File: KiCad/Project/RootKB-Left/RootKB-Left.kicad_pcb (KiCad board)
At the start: 2 copper layers, 137.4 x 107.4 mm, 69 parts, among them J1 OLED-128x32, U1 Arduino_Pro_Micro, U2 TRRS

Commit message: add jblpcb order number location
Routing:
- added copper zone on B.Cu, net GND
- added copper zone on F.Cu, net GND
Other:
- board text added: "JLCJLCJLCJLC"
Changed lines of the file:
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@@
 		(layer "User.9")
 	)
+	(gr_text "JLCJLCJLCJLC"
+		(at 138.934292 116.834545 331)
+		(layer "B.SilkS")
+		(effects
+			(font
+				(size 1 1)
+				(thickness 0.25)
+				(bold yes)
+			)
+			(justify left bottom mirror)
+		)
+	)
 	(gr_text "by Matei Ionescu"
 		(at 127.988 113.0215 331)
@@
 		(net 64)
 	)
-	(group ""
-		(members "570610eb-6886-4a19-860b-f766abbdb514")
+	(zone
+		(net 32)
+		(net_name "GND")
+		(layers "F&B.Cu")
+		(hatch edge 0.5)
+		(connect_pads
+			(clearance 0)
+		)
+		(min_thickness 0.25)
+		(filled_areas_thickness no)
+		(fill yes
+			(thermal_gap 0.5)
+			(thermal_bridge_width 0.5)
+		)
+		(polygon
+			(pts
+				(xy 69.934292 32.634545) (xy 69.934292 152.634545) (xy 224.934292 152.634545) (xy 224.934292 32.634545)
+			)
+		)
 	)
 	(group ""

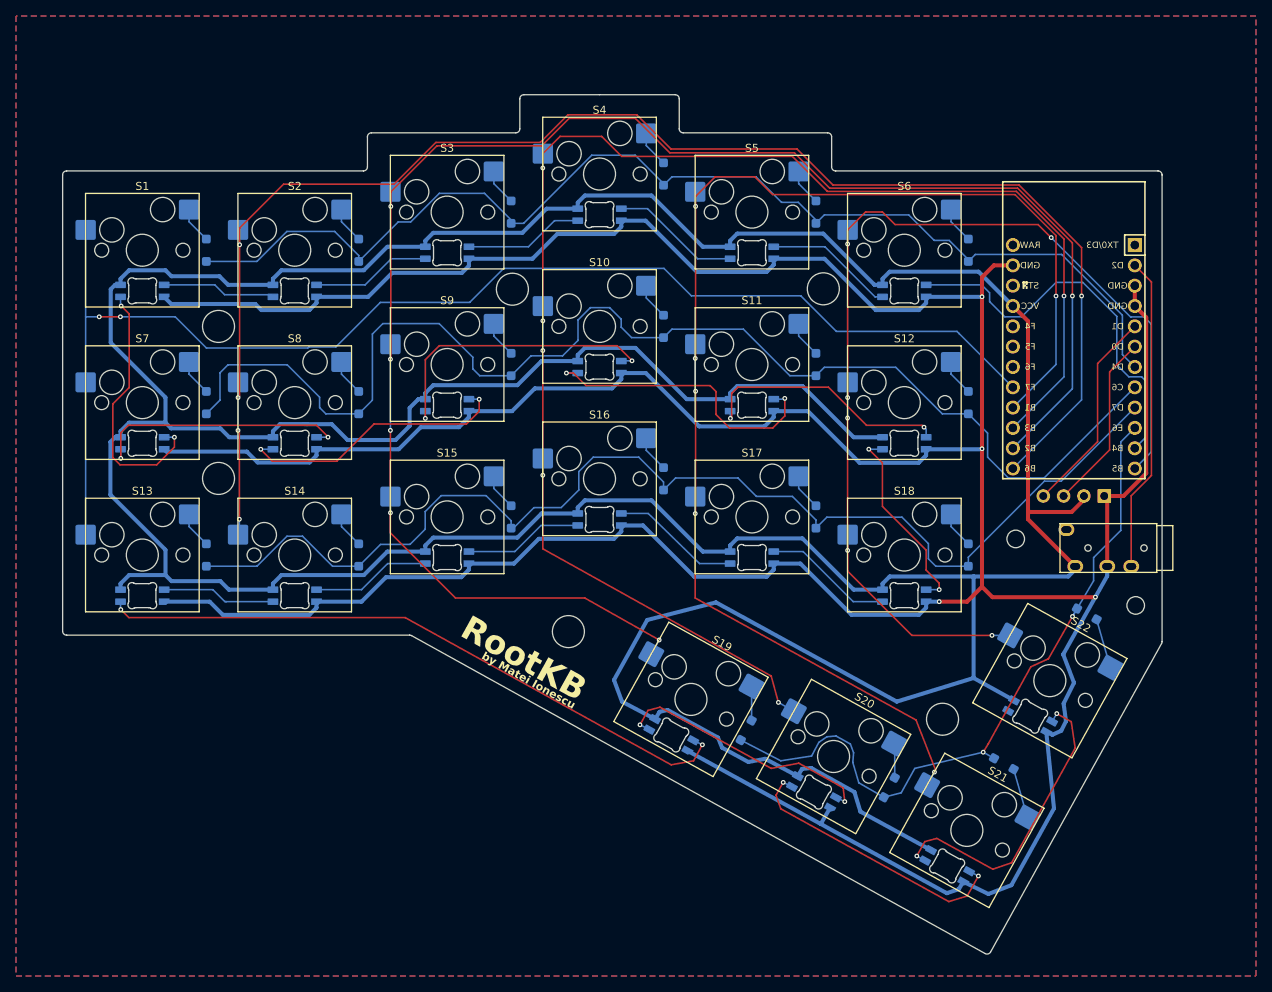
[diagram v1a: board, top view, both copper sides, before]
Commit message: use UART
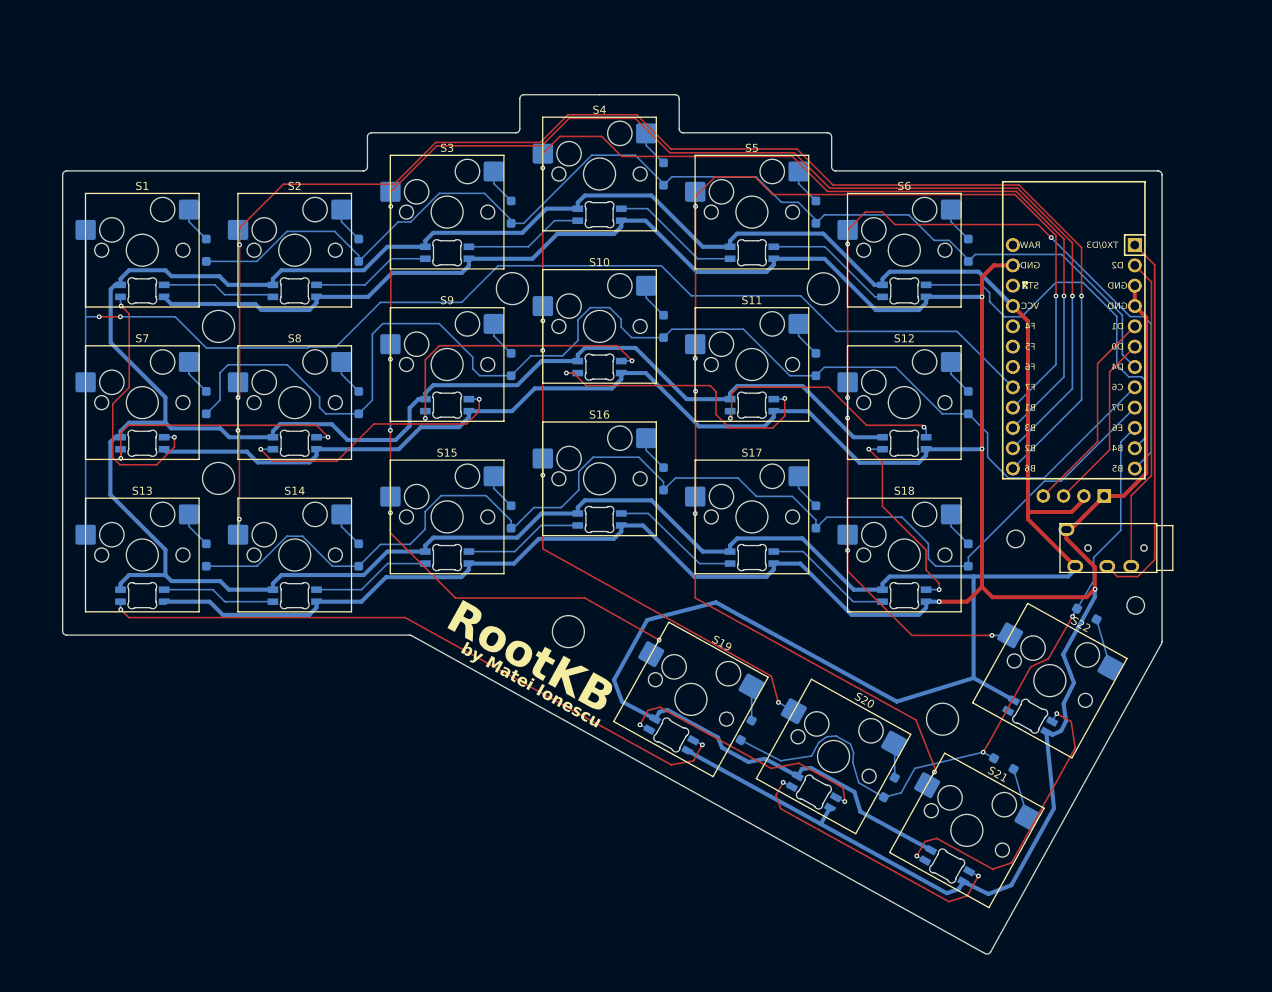
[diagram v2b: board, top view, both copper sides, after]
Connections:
- net TRRS_SERIAL renamed TRRS_RX
- U1 pad 1: unconnected-(U1-TX0/PD3-Pad1) -> TRRS_TX
- U2 pad 1: unconnected-(U2-SLEEVE-Pad1) -> GND
- U2 pad 3: GND -> TRRS_TX
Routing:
- net TRRS_TX: track 0.00 -> 47.8 mm
- net GND: track 541.8 -> 545.7 mm
- removed copper zone on B.Cu, net GND
- removed copper zone on F.Cu, net GND
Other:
- outline, holes or cut-outs redrawn

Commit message: add titles
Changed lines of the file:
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@@
 	)
 	(paper "A4")
+	(title_block
+		(title "RootKB-Left PCB")
+		(date "2024-05-05")
+		(rev "1.0")
+	)
 	(layers
 		(0 "F.Cu" signal)
@@
 		(fp_arc
 			(start 1.749484 0.919721)
-			(mid 1.712534 0.814067)
+			(mid 1.71254 0.814067)
 			(end 1.699999 0.702843)
 			(stroke
@@
 		(fp_arc
 			(start -1.046711 1.568299)
-			(mid -1.63807 1.504035)
+			(mid -1.638071 1.504035)
 			(end -1.749484 0.919721)
 			(stroke
@@
 		(fp_arc
 			(start 1.749484 0.919721)
-			(mid 1.712534 0.814067)
+			(mid 1.71254 0.814067)
 			(end 1.699999 0.702843)
 			(stroke
@@
 		(fp_arc
 			(start -1.046711 1.568299)
-			(mid -1.63807 1.504035)
+			(mid -1.638071 1.504035)
 			(end -1.749484 0.919721)
 			(stroke
@@
 		(fp_arc
 			(start 1.749484 0.919721)
-			(mid 1.712534 0.814067)
+			(mid 1.71254 0.814067)
 			(end 1.699999 0.702843)
 			(stroke
@@
 		(fp_arc
 			(start -1.046711 1.568299)
-			(mid -1.63807 1.504035)
+			(mid -1.638071 1.504035)
 			(end -1.749484 0.919721)
 			(stroke
@@
 		(fp_arc
 			(start 1.749484 0.919721)
-			(mid 1.712534 0.814067)
+			(mid 1.71254 0.814067)
 			(end 1.699999 0.702843)
 			(stroke
@@
 		(fp_arc
 			(start -1.046711 1.568299)
-			(mid -1.63807 1.504035)
+			(mid -1.638071 1.504035)
 			(end -1.749484 0.919721)
 			(stroke
@@
 		(fp_arc
 			(start 1.749484 0.919721)
-			(mid 1.712534 0.814067)
+			(mid 1.71254 0.814067)
 			(end 1.699999 0.702843)
 			(stroke
@@
 		(fp_arc
 			(start -1.046711 1.568299)
-			(mid -1.63807 1.504035)
+			(mid -1.638071 1.504035)
 			(end -1.749484 0.919721)
 			(stroke
@@
 		(fp_arc
 			(start 1.699999 -0.702841)
-			(mid 1.712538 -0.814065)
+			(mid 1.712537 -0.814064)
 			(end 1.749485 -0.919718)
 			(stroke
@@
 		(fp_arc
 			(start 1.749484 0.919721)
-			(mid 1.712534 0.814067)
+			(mid 1.712541 0.814066)
 			(end 1.699999 0.702843)
 			(stroke
@@
 		(fp_arc
 			(start 0.794453 1.500001)
-			(mid 0.925123 1.517379)
+			(mid 0.925123 1.51738)
 			(end 1.046711 1.5683)
 			(stroke
@@
 		(fp_arc
 			(start 1.699999 -0.702841)
-			(mid 1.712538 -0.814065)
+			(mid 1.712537 -0.814064)
 			(end 1.749485 -0.919718)
 			(stroke
@@
 		(fp_arc
 			(start 1.749484 0.919721)
-			(mid 1.712534 0.814067)
+			(mid 1.712541 0.814066)
 			(end 1.699999 0.702843)
 			(stroke
@@
 		(fp_arc
 			(start 0.794453 1.500001)
-			(mid 0.925123 1.517379)
+			(mid 0.925123 1.51738)
 			(end 1.046711 1.5683)
 			(stroke
@@
 		(fp_arc
 			(start 1.749484 0.919721)
-			(mid 1.712534 0.814067)
+			(mid 1.71254 0.814067)
 			(end 1.699999 0.702843)
 			(stroke
@@
 		(fp_arc
 			(start -1.046711 1.568299)
-			(mid -1.63807 1.504035)
+			(mid -1.638071 1.504035)
 			(end -1.749484 0.919721)
 			(stroke
@@
 		(fp_arc
 			(start 1.749484 0.919721)
-			(mid 1.712534 0.814067)
+			(mid 1.71254 0.814067)
 			(end 1.699999 0.702843)
 			(stroke
@@
 		(fp_arc
 			(start -1.046711 1.568299)
-			(mid -1.63807 1.504035)
+			(mid -1.638071 1.504035)
 			(end -1.749484 0.919721)
 			(stroke
@@
 		(fp_arc
 			(start 1.749484 0.919721)
-			(mid 1.712534 0.814067)
+			(mid 1.71254 0.814067)
 			(end 1.699999 0.702843)
 			(stroke
@@
 		(fp_arc
 			(start -1.046711 1.568299)
-			(mid -1.63807 1.504035)
+			(mid -1.638071 1.504035)
 			(end -1.749484 0.919721)
 			(stroke
@@
 		(fp_arc
 			(start 1.749484 0.919721)
-			(mid 1.712534 0.814067)
+			(mid 1.71254 0.814067)
 			(end 1.699999 0.702843)
 			(stroke
@@
 		(fp_arc
 			(start -1.046711 1.568299)
-			(mid -1.63807 1.504035)
+			(mid -1.638071 1.504035)
 			(end -1.749484 0.919721)
 			(stroke
@@
 		(fp_arc
 			(start 1.749484 0.919721)
-			(mid 1.712534 0.814067)
+			(mid 1.71254 0.814067)
 			(end 1.699999 0.702843)
 			(stroke
@@
 		(fp_arc
 			(start -1.046711 1.568299)
-			(mid -1.63807 1.504035)
+			(mid -1.638071 1.504035)
 			(end -1.749484 0.919721)
 			(stroke
@@
 		(fp_arc
 			(start 1.699999 -0.702841)
-			(mid 1.712538 -0.814065)
+			(mid 1.712537 -0.814064)
 			(end 1.749485 -0.919718)
 			(stroke
@@
 		(fp_arc
 			(start 1.749484 0.919721)
-			(mid 1.712534 0.814067)
+			(mid 1.712541 0.814066)
 			(end 1.699999 0.702843)
 			(stroke
@@
 		(fp_arc
 			(start 0.794453 1.500001)
-			(mid 0.925123 1.517379)
+			(mid 0.925123 1.51738)
 			(end 1.046711 1.5683)
 			(stroke
@@
 		(fp_arc
 			(start 1.749484 0.919721)
-			(mid 1.712534 0.814067)
+			(mid 1.71254 0.814067)
 			(end 1.699999 0.702843)
 			(stroke
@@
 		(fp_arc
 			(start -1.046711 1.568299)
-			(mid -1.63807 1.504035)
+			(mid -1.638071 1.504035)
 			(end -1.749484 0.919721)
 			(stroke
@@
 		(fp_arc
 			(start 1.699999 -0.702841)
-			(mid 1.712538 -0.814065)
+			(mid 1.712537 -0.814064)
 			(end 1.749485 -0.919718)
 			(stroke
@@
 		(fp_arc
 			(start 1.749484 0.919721)
-			(mid 1.712534 0.814067)
+			(mid 1.712541 0.814066)
 			(end 1.699999 0.702843)
 			(stroke
@@
 		(fp_arc
 			(start 0.794453 1.500001)
-			(mid 0.925123 1.517379)
+			(mid 0.925123 1.51738)
 			(end 1.046711 1.5683)
 			(stroke
@@
 		(fp_arc
 			(start 1.749484 0.919721)
-			(mid 1.712534 0.814067)
+			(mid 1.71254 0.814067)
 			(end 1.699999 0.702843)
 			(stroke
@@
 		(fp_arc
 			(start -1.046711 1.568299)
-			(mid -1.63807 1.504035)
+			(mid -1.638071 1.504035)
 			(end -1.749484 0.919721)
 			(stroke
@@
 		(fp_arc
 			(start 1.749484 0.919721)
-			(mid 1.712534 0.814067)
+			(mid 1.71254 0.814067)
 			(end 1.699999 0.702843)
 			(stroke
@@
 		(fp_arc
 			(start -1.046711 1.568299)
-			(mid -1.63807 1.504035)
+			(mid -1.638071 1.504035)
 			(end -1.749484 0.919721)
 			(stroke
@@
 		(fp_arc
 			(start 1.749484 0.919721)
-			(mid 1.712534 0.814067)
+			(mid 1.71254 0.814067)
 			(end 1.699999 0.702843)
 			(stroke
@@
 		(fp_arc
 			(start -1.046711 1.568299)
-			(mid -1.63807 1.504035)
+			(mid -1.638071 1.504035)
 			(end -1.749484 0.919721)
 			(stroke
@@
 		(fp_arc
 			(start 1.749484 0.919721)
-			(mid 1.712534 0.814067)
+			(mid 1.71254 0.814067)
 			(end 1.699999 0.702843)
 			(stroke
@@
 		(fp_arc
 			(start -1.046711 1.568299)
-			(mid -1.63807 1.504035)
+			(mid -1.638071 1.504035)
 			(end -1.749484 0.919721)
 			(stroke
@@
 		(fp_arc
 			(start 1.749484 0.919721)
-			(mid 1.712534 0.814067)
+			(mid 1.71254 0.814067)
 			(end 1.699999 0.702843)
 			(stroke
@@
 		(fp_arc
 			(start -1.046711 1.568299)
-			(mid -1.63807 1.504035)
+			(mid -1.638071 1.504035)
 			(end -1.749484 0.919721)
 			(stroke
@@
 		(fp_arc
 			(start 1.749484 0.919721)
-			(mid 1.712534 0.814067)
+			(mid 1.71254 0.814067)
 			(end 1.699999 0.702843)
 			(stroke
@@
 		(fp_arc
 			(start -1.046711 1.568299)
-			(mid -1.63807 1.504035)
+			(mid -1.638071 1.504035)
 			(end -1.749484 0.919721)
 			(stroke
@@
 		(fp_arc
 			(start 1.749484 0.919721)
-			(mid 1.712534 0.814067)
+			(mid 1.71254 0.814067)
 			(end 1.699999 0.702843)
 			(stroke
@@
 		(fp_arc
 			(start -1.046711 1.568299)
-			(mid -1.63807 1.504035)
+			(mid -1.638071 1.504035)
 			(end -1.749484 0.919721)
 			(stroke

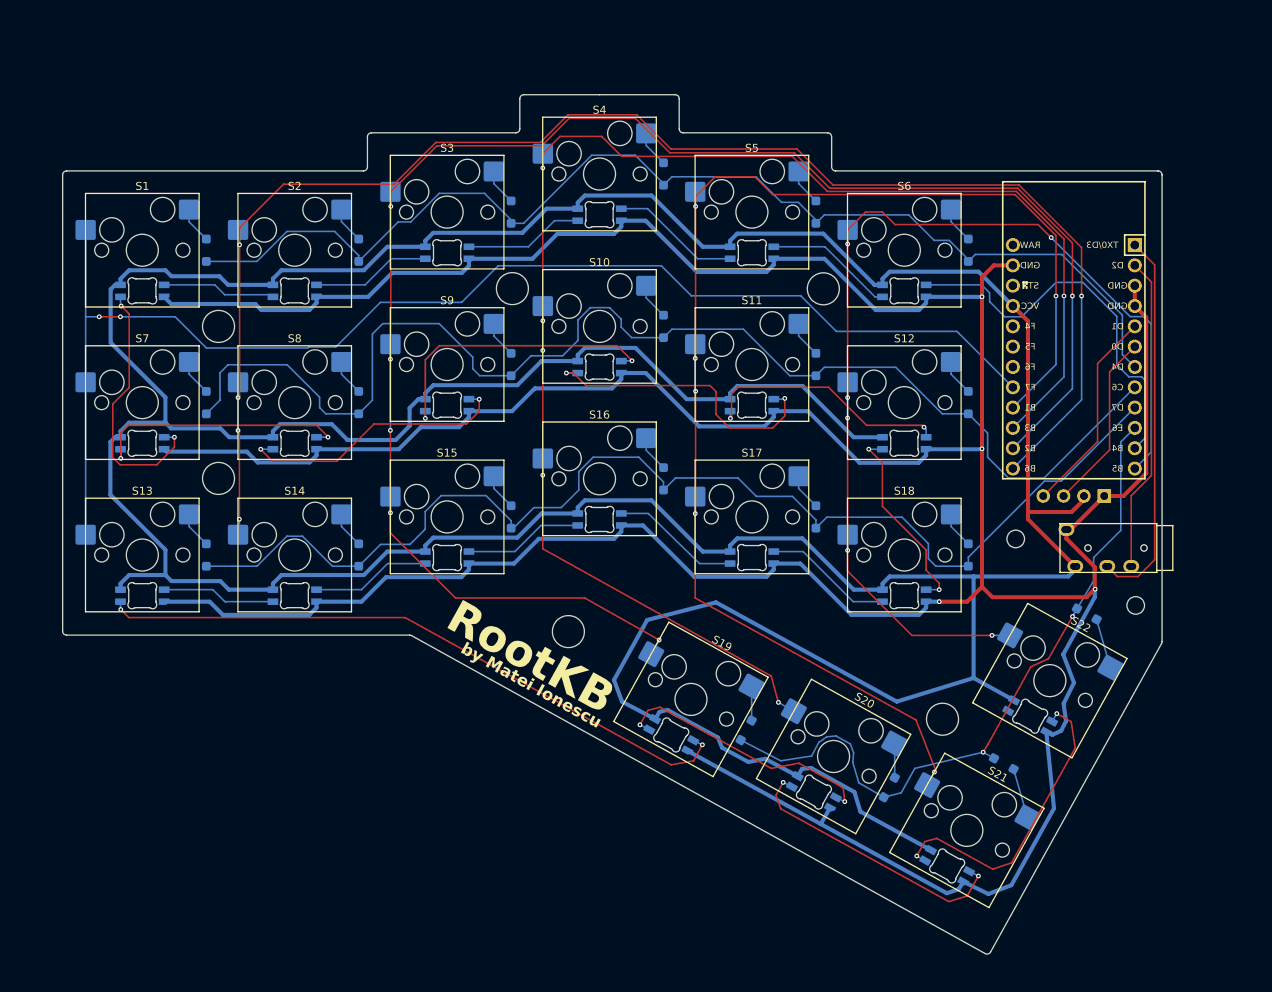
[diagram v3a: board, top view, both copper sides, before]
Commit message: update routes
more clearance for some routes
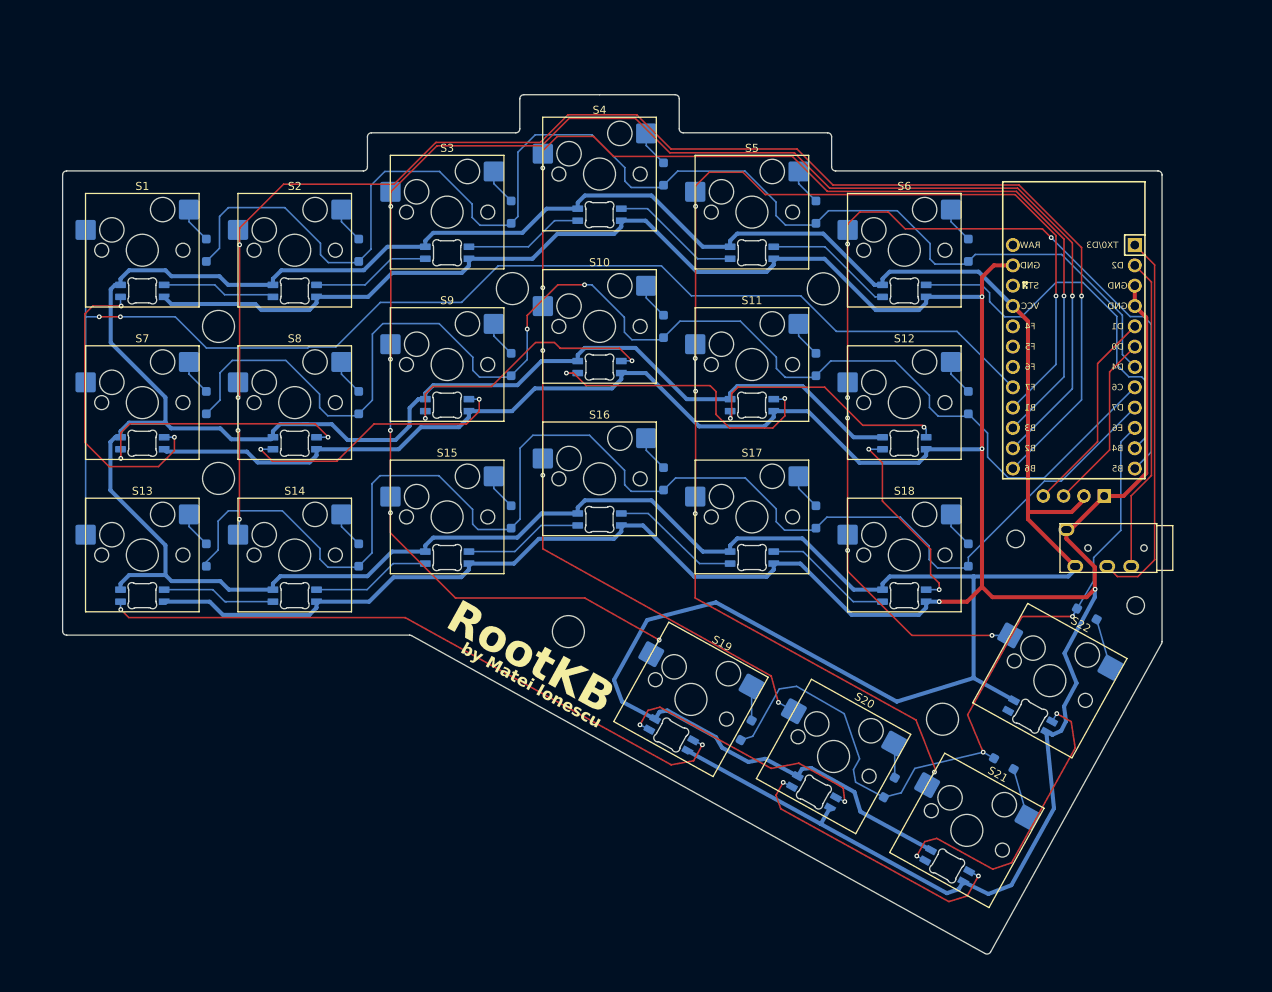
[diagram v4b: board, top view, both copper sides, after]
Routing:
- net Row 0: track 145.3 -> 169.6 mm
- net Row 2: track 150.6 -> 170.4 mm
- net Row 3: track 88.9 -> 99.6 mm
- net Row 1: track 159.6 -> 169.2 mm, vias 0 -> 2
- net Net-(LED1-DOUT): track 32.9 -> 38.4 mm
- net Net-(LED10-DIN): track 36.9 -> 34.8 mm
- net Column 4: track 169.3 -> 170.5 mm
- net Column 3: track 193.5 -> 194.1 mm

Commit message: minor routing changes
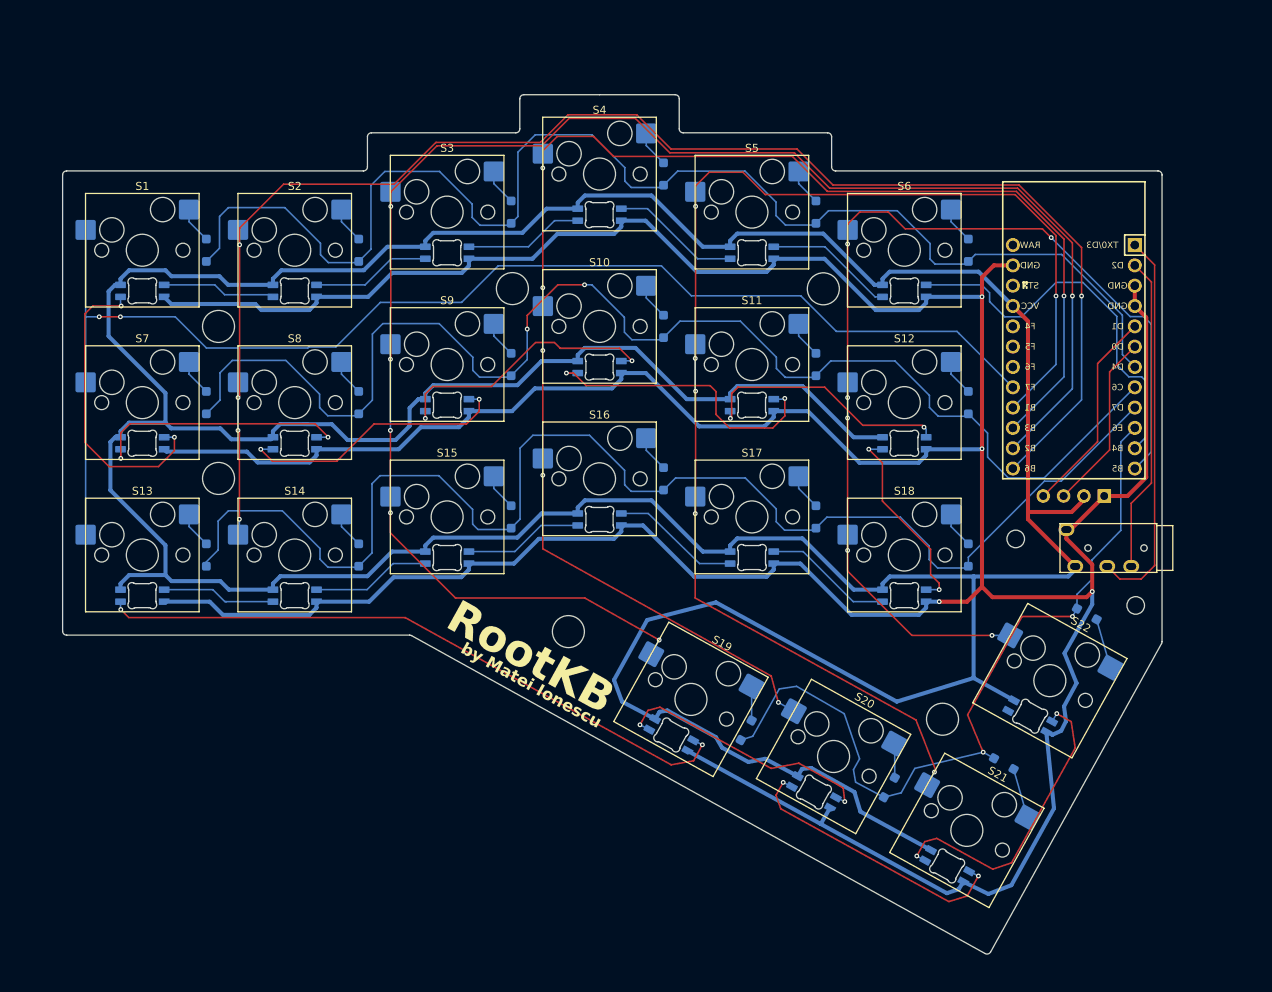
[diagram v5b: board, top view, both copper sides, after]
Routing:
- net Row 3: track 99.6 -> 98.7 mm
- net TRRS_TX: track 47.8 -> 48.5 mm

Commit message: update routing
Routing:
- net LED: track 49.2 -> 58.6 mm, vias 0 -> 2
- net Column 5: track 135.9 -> 143.5 mm
- net Row 2: track 170.4 -> 173.0 mm
- net Row 1: track 169.2 -> 170.6 mm

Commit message: last updates
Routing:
- net Row 0: track 169.6 -> 172.0 mm
- net Column 5: track 143.5 -> 144.3 mm
